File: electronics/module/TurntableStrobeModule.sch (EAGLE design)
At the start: 11 parts, among them IC1 TINY25, J1 ISP, Q1 12MHz

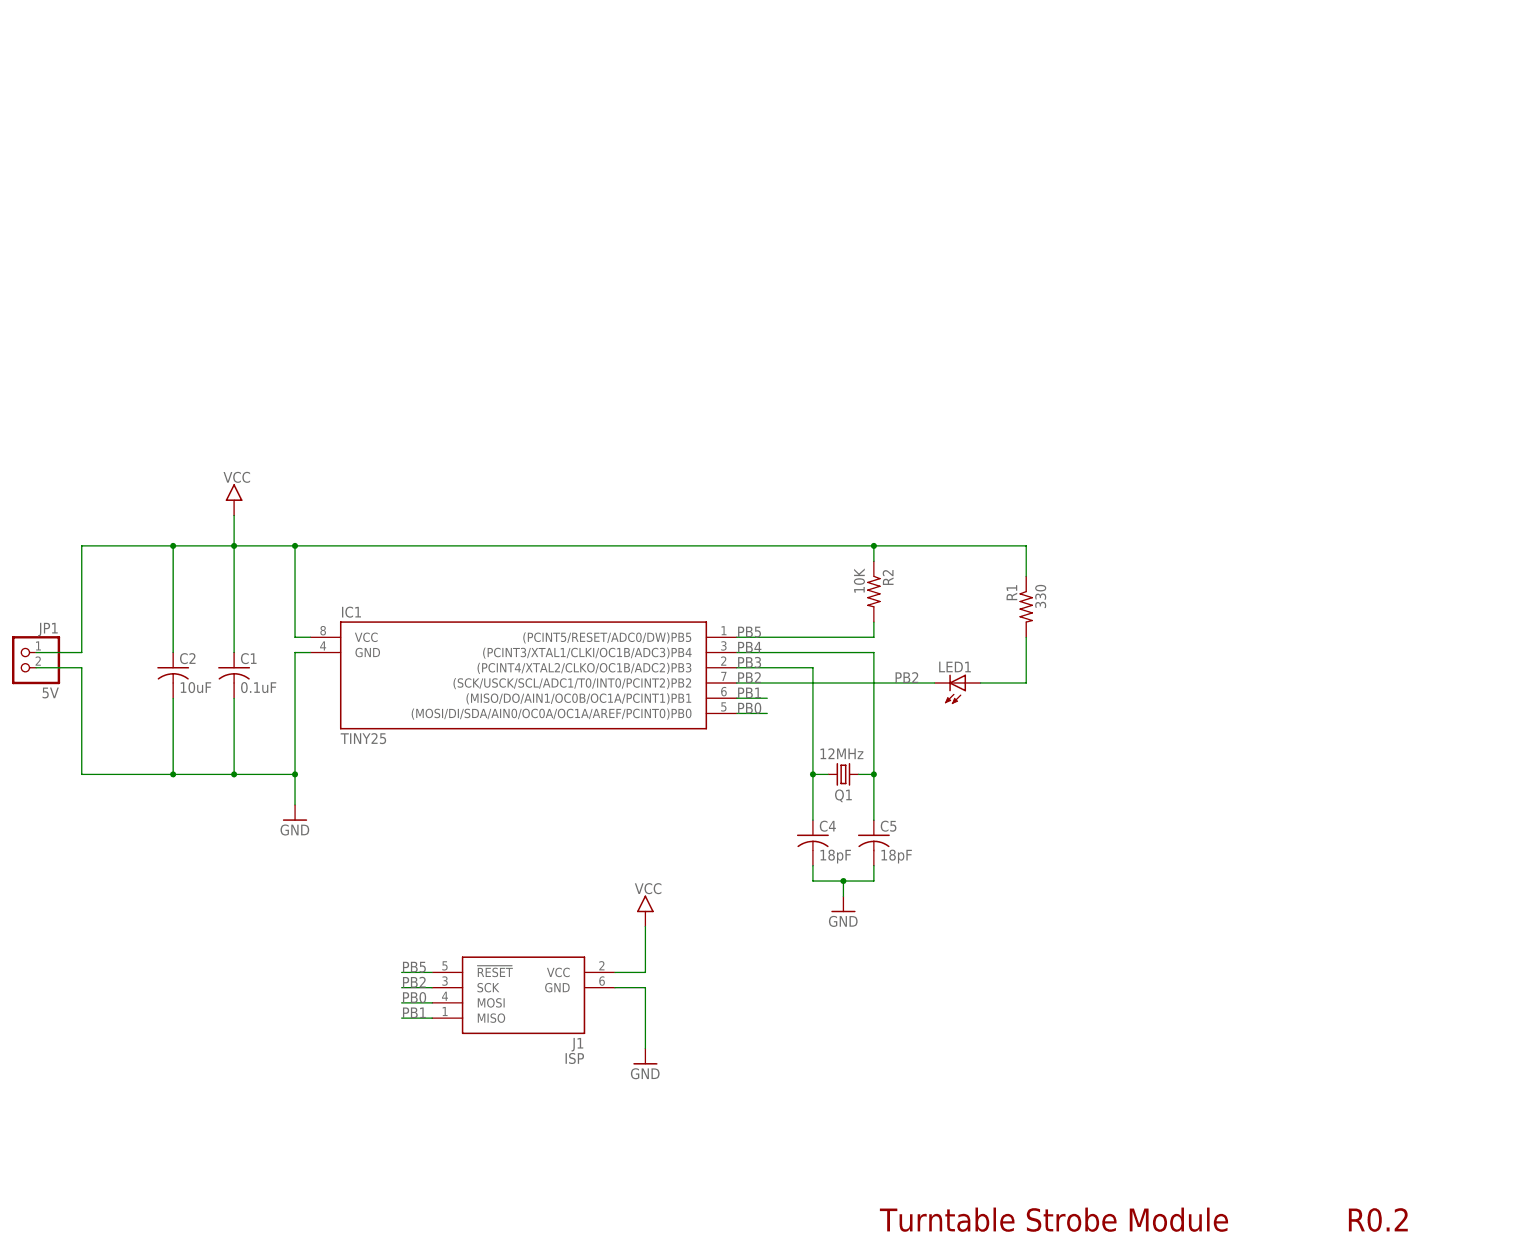
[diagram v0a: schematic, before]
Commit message: added regulator onboard, changed some packages
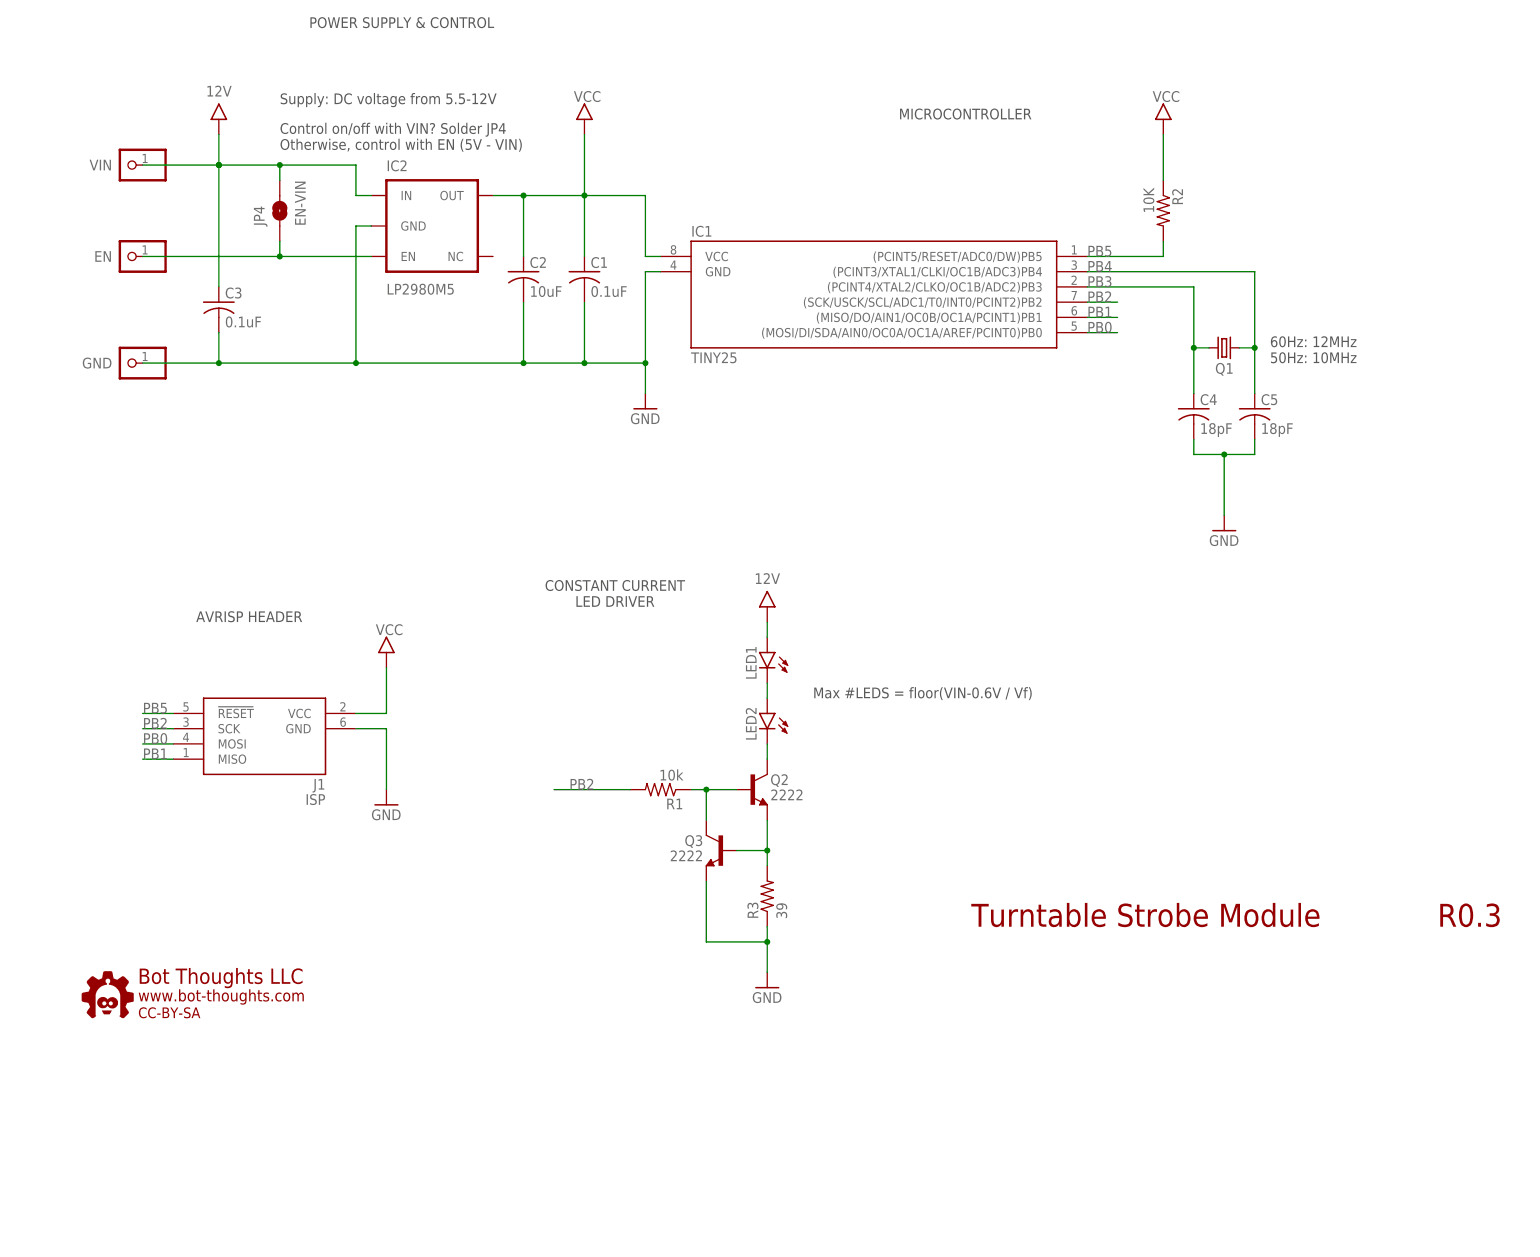
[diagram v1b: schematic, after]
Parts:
- added C3: 0.1uF, bt_rcl:C-0603
- added IC2: LP2980M5, bt_regulator:LP2980M5
- added JP2: VIN, bt_electromech:PINHD-1X01_2.54-S
- added JP3: GND, bt_electromech:PINHD-1X01_2.54-S
- added JP4: EN-VIN, SparkFun-Jumpers:JUMPER-SMT_2_NO_SILK
- added LED2: (no value), bt_opto:LED5MMRA
- added Q2, Q3: 2222, bt_transistor:BJT-NPNSOT23
- added R3: 39, bt_rcl:R0603
- added U$6: BTLOGO-LOGO-MD, bt:BTLOGO-LOGO-MD
- C1, C4, C5: device rcl:C-USC0603 -> bt_rcl:C-0603
- C2: device rcl:C-USC1206 -> bt_rcl:C-1206
- JP1: value 5V -> EN; device pinhead-2:PINHD-1X02_2.54-S -> bt_electromech:PINHD-1X01_2.54-S
- Q1: value 12MHz -> (none)
- R1: value 330 -> 10k; device rcl:R-US_R0603 -> bt_rcl:R0603
- R2: device rcl:R-US_R0603 -> bt_rcl:R0603
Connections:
- new net 9V: C3.+, IC2.IN, JP2.1, JP4.2, LED1.A
- new net N$1: Q2.B, Q3.C, R1.1
- new net N$2: LED1.C, LED2.A
- new net N$4: Q2.E, Q3.B, R3.2
- new net N$5: IC2.EN, JP1.1, JP4.1
- net GND: now also C1.-, C2.-, C3.-, C4.-, C5.-, IC2.GND, JP3.1, Q3.E, R3.1; no longer C1.2, C2.2, C4.2, C5.2, JP1.2
- net N$3: now also LED2.C, Q2.C; no longer LED1.A, R1.2
- net PB2: now also R1.2; no longer LED1.C
- net PB3: now also C4.+; no longer C4.1
- net PB4: now also C5.+; no longer C5.1
- net VCC: now also C1.+, C2.+, IC2.OUT; no longer C1.1, C2.1, JP1.1, R1.1
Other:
- note added: "60Hz: 12MHz 50Hz: 10MHz"
- note added: "AVRISP HEADER"
- note added: "CONSTANT CURRENT LED DRIVER"
- note added: "Control on/off with VIN? Solder JP4 Otherwise, control with EN (5V - VIN)"
- note added: "MICROCONTROLLER"
- note added: "Max #LEDS = floor(VIN-0.6V / Vf)"
- note added: "POWER SUPPLY & CONTROL"
- note added: "R0.3"
- note added: "Supply: DC voltage from 5.5-12V"
- note removed: "R0.2"
- moved on the sheet: IC1, J1, Q1
